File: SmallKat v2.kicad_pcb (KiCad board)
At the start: 4 copper layers, 104 x 56 mm, 272 parts, among them IC1 TPS562201DDCR, IC2 TPS40192DRCT, IC4 MAX34409ETE+, IC5 MAX34409ETE+, IC6 MAX34409ETE+, IC7 MAX34409ETE+, J1 Conn_01x03_Male, J10 Conn_01x03_Male, J11 Conn_01x03_Male, J12 Conn_01x03_Male, J13 Conn_01x03_Male, J14 Conn_01x03_Male, J15 Conn_01x03_Male, J16 Conn_01x03_Male, J17 Conn_01x03_Male, J19 USB_C_Receptacle, J2 Conn_01x03_Male, J21 Conn_01x05_Male, J3 Conn_01x03_Male, J4 Conn_01x03_Male, J5 Conn_01x03_Male, J6 Conn_01x03_Male, J7 Conn_01x03_Male, J8 Conn_01x03_Male, J9 Conn_01x02_Male, Q1 BUK9M120-100EX, Q10 CSD17307Q5A, Q11 CSD17307Q5A, Q12 Si7141DP, Q2 BUK9M120-100EX, Q3 MMBT3904, Q4 MMBT3904, Q7 2N3905, Q8 BUK9M120-100EX, Q9 BUK9M120-100EX, SW1 SW_SPST, SW2 SW_SPST, SW5 SW_SPST, U1 BNO055, U11 FUSB302BMPX, U12 BQ24770, U13 bq76925, U14 PCA9641, U2 LM2840Y, U3 ESP32-WROOM-32, U4 CP2102N-A01-GQFN24, U6 STM32L432KBUx, Y1 32.768kHz

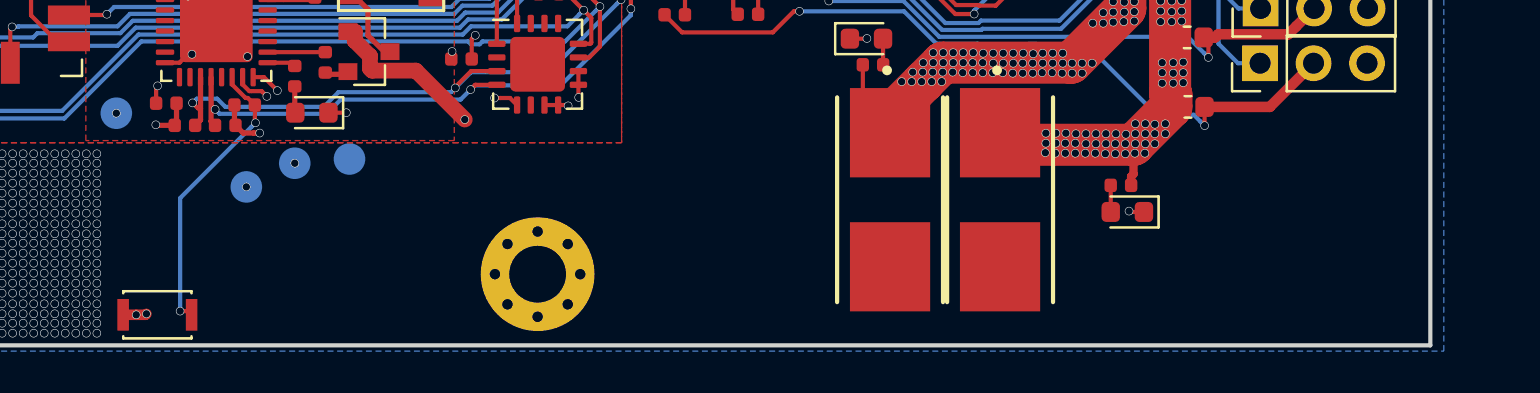
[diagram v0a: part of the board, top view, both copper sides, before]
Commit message: added version to silk
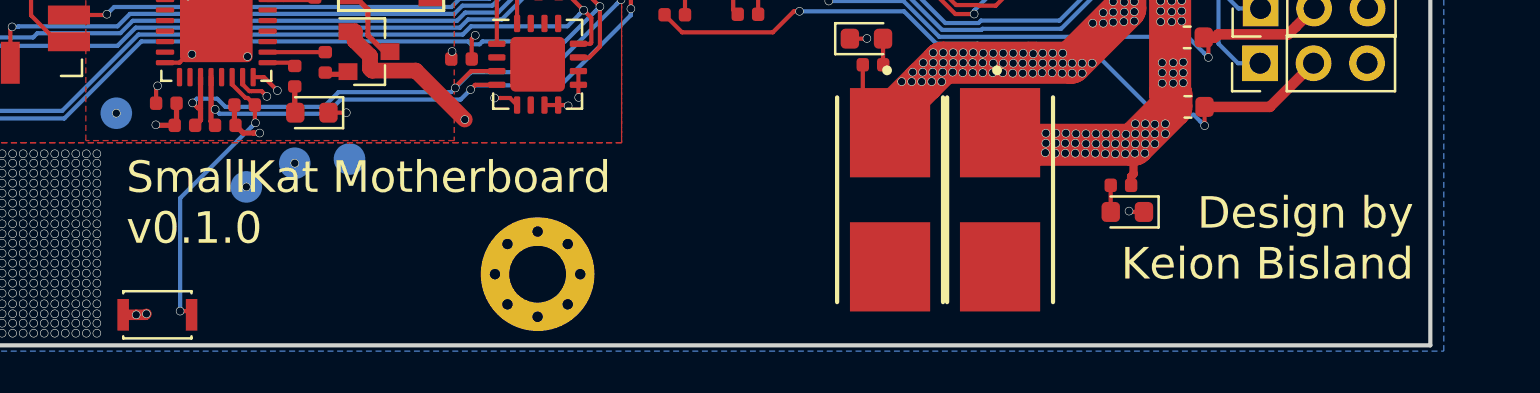
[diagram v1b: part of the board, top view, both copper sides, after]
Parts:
- L2: footprint Inductor_SMD:L_Bourns_SRP1245A -> L_Bourns_SRP1245A:L_Bourns_SRP1245A
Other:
- board text added: "Design by Keion Bisland"
- board text added: "SmallKat Motherboard v0.1.0"
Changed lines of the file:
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@@
   (general
     (thickness 1.6)
-    (drawings 23)
+    (drawings 25)
     (tracks 5690)
     (zones 0)
@@
       (drillshape 0)
       (scaleselection 1)
-      (outputdirectory "GERBER/"))
+      (outputdirectory "GERBER-t/"))
   )
   (net 0 "")
@@
     (add_net VBUS)
   )
+  (module L_Bourns_SRP1245A:L_Bourns_SRP1245A (layer F.Cu)
+    (at 135.8 94.3 180)
+    (descr "Bourns SRP1245A series SMD inductor http://www.bourns.com/docs/Product-Datasheets/SRP1245A.pdf")
+    (tags "Bourns SRP1245A SMD inductor")
+    (attr smd)
+    (fp_text reference L2 (at 0 -7.25 unlocked) (layer F.SilkS) hide
+      (effects (font (size 1 1) (thickness 0.15)))
+    )
+    (fp_text value 1uH (at 0 7.4 unlocked) (layer F.Fab) hide
+      (effects (font (size 1 1) (thickness 0.15)))
+    )
+    (fp_line (start -7.35 -2.75) (end -6.55 -2.75) (layer F.CrtYd) (width 0.05))
+    (fp_line (start -6.55 5.7) (end -6.55 2.75) (layer F.CrtYd) (width 0.05))
+    (fp_line (start -6.55 -2.75) (end -6.55 -5.7) (layer F.CrtYd) (width 0.05))
+    (fp_line (start -7.35 2.75) (end -6.55 2.75) (layer F.CrtYd) (width 0.05))
+    (fp_line (start -7.35 2.75) (end -7.35 -2.75) (layer F.CrtYd) (width 0.05))
+    (fp_line (start 6.55 2.75) (end 6.55 5.7) (layer F.CrtYd) (width 0.05))
+    (fp_line (start 6.55 -5.7) (end 6.55 -2.75) (layer F.CrtYd) (width 0.05))
+    (fp_line (start 7.35 -2.75) (end 7.35 2.75) (layer F.CrtYd) (width 0.05))
+    (fp_line (start 7.35 -2.75) (end 6.55 -2.75) (layer F.CrtYd) (width 0.05))
+    (fp_line (start 7.35 2.75) (end 6.55 2.75) (layer F.CrtYd) (width 0.05))
+    (fp_line (start -5.75 -6.25) (end 5.75 -6.25) (layer F.Fab) (width 0.1))
+    (fp_line (start -6.3 -5.75) (end -6.3 5.7) (layer F.Fab) (width 0.1))
+    (fp_line (start 5.75 6.25) (end -5.75 6.25) (layer F.Fab) (width 0.1))
+    (fp_line (start 6.3 -5.7) (end 6.3 5.7) (layer F.Fab) (width 0.1))
+    (fp_line (start -5.75 -6.4) (end 5.75 -6.4) (layer F.SilkS) (width 0.12))
+    (fp_line (start -6.45 -5.75) (end -6.45 -2.8) (layer F.SilkS) (width 0.12))
+    (fp_line (start 5.75 6.4) (end -5.75 6.4) (layer F.SilkS) (width 0.12))
+    (fp_line (start 6.45 -5.7) (end 6.45 -2.8) (layer F.SilkS) (width 0.12))
+    (fp_line (start -5.75 -6.5) (end 5.75 -6.5) (layer F.CrtYd) (width 0.05))
+    (fp_line (start 5.75 6.5) (end -5.75 6.5) (layer F.CrtYd) (width 0.05))
+    (fp_text user %R (at 0 0 unlocked) (layer F.Fab) hide
+      (effects (font (size 1 1) (thickness 0.15)))
+    )
+    (fp_arc (start -5.75 -5.7) (end -5.75 -6.25) (angle -90) (layer F.Fab) (width 0.1))
+    (fp_arc (start 5.75 -5.7) (end 6.3 -5.7) (angle -90) (layer F.Fab) (width 0.1))
+    (fp_arc (start 5.75 5.7) (end 5.75 6.25) (angle -90) (layer F.Fab) (width 0.1))
+    (fp_arc (start -5.75 5.7) (end -6.3 5.7) (angle -90) (layer F.Fab) (width 0.1))
+    (fp_line (start -6.45 2.8) (end -6.45 5.7) (layer F.SilkS) (width 0.12))
+    (fp_line (start 6.45 2.8) (end 6.45 5.7) (layer F.SilkS) (width 0.12))
+    (fp_arc (start -5.75 -5.7) (end -5.75 -6.4) (angle -90) (layer F.SilkS) (width 0.12))
+    (fp_arc (start -5.75 5.7) (end -6.45 5.7) (angle -90) (layer F.SilkS) (width 0.12))
+    (fp_arc (start 5.75 5.7) (end 5.75 6.4) (angle -90) (layer F.SilkS) (width 0.12))
+    (fp_arc (start 5.75 -5.7) (end 6.45 -5.7) (angle -90) (layer F.SilkS) (width 0.12))
+    (fp_arc (start -5.75 -5.7) (end -5.75 -6.5) (angle -90) (layer F.CrtYd) (width 0.05))
+    (fp_arc (start -5.75 5.7) (end -6.55 5.7) (angle -90) (layer F.CrtYd) (width 0.05))
+    (fp_arc (start 5.75 5.7) (end 5.75 6.5) (angle -90) (layer F.CrtYd) (width 0.05))
+    (fp_arc (start 5.75 -5.7) (end 6.55 -5.7) (angle -90) (layer F.CrtYd) (width 0.05))
+    (pad 2 smd rect (at 6.5 0 180) (size 3.1 5) (layers F.Cu F.Paste F.Mask)
+      (net 4 +6V))
+    (pad 1 smd rect (at -6.5 0 180) (size 3.1 5) (layers F.Cu F.Paste F.Mask)
+      (net 22 "Net-(C15-Pad1)"))
+    (model ${KISYS3DMOD}/Inductor_SMD.3dshapes/L_Bourns_SRP1245A.wrl
+      (at (xyz 0 0 0))
+      (scale (xyz 1 1 1))
+      (rotate (xyz 0 0 0))
+    )
+    (model "${KIPRJMOD}/L_Bourns_SRP1245A/SRP1245A series.stp"
+      (at (xyz 0 0 0))
+      (scale (xyz 1 1 1))
+      (rotate (xyz 0 0 0))
+    )
+  )
   (module USB_C_Receptacle_Amphenol_12401610E4-2A:USB_C_Receptacle_Amphenol_12401610E4-2A_CircularHoles (layer F.Cu)
     (at 171.18 92.09 180)
@@
       (rotate (xyz 0 0 0))
     )
+    (model ${KIPRJMOD}/USB_C_Receptacle_Amphenol_12401610E4-2A/12401610E4#2A--3DModel-STEP-56544.STEP
+      (offset (xyz 0 -5.25 1.5))
+      (scale (xyz 1 1 1))
+      (rotate (xyz -90 0 0))
+    )
   )
   (module 0154:0154.250DR (layer F.Cu)
@@
     (pad "" smd rect (at 1.95 -1.65) (size 1.2 0.7) (layers F.Cu F.Paste F.Mask))
   )
-  (module Inductor_SMD:L_Bourns_SRP1245A (layer F.Cu)
-    (at 135.8 94.3 180)
-    (descr "Bourns SRP1245A series SMD inductor http://www.bourns.com/docs/Product-Datasheets/SRP1245A.pdf")
-    (tags "Bourns SRP1245A SMD inductor")
-    (attr smd)
-    (fp_text reference L2 (at 0 -7.25 unlocked) (layer F.SilkS) hide
-      (effects (font (size 1 1) (thickness 0.15)))
-    )
-    (fp_text value 1uH (at 0 7.4 unlocked) (layer F.Fab) hide
-      (effects (font (size 1 1) (thickness 0.15)))
-    )
-    (fp_line (start -7.35 -2.75) (end -6.55 -2.75) (layer F.CrtYd) (width 0.05))
-    (fp_line (start -6.55 5.7) (end -6.55 2.75) (layer F.CrtYd) (width 0.05))
-    (fp_line (start -6.55 -2.75) (end -6.55 -5.7) (layer F.CrtYd) (width 0.05))
-    (fp_line (start -7.35 2.75) (end -6.55 2.75) (layer F.CrtYd) (width 0.05))
-    (fp_line (start -7.35 2.75) (end -7.35 -2.75) (layer F.CrtYd) (width 0.05))
-    (fp_line (start 6.55 2.75) (end 6.55 5.7) (layer F.CrtYd) (width 0.05))
-    (fp_line (start 6.55 -5.7) (end 6.55 -2.75) (layer F.CrtYd) (width 0.05))
-    (fp_line (start 7.35 -2.75) (end 7.35 2.75) (layer F.CrtYd) (width 0.05))
-    (fp_line (start 7.35 -2.75) (end 6.55 -2.75) (layer F.CrtYd) (width 0.05))
-    (fp_line (start 7.35 2.75) (end 6.55 2.75) (layer F.CrtYd) (width 0.05))
-    (fp_line (start -5.75 -6.25) (end 5.75 -6.25) (layer F.Fab) (width 0.1))
-    (fp_line (start -6.3 -5.75) (end -6.3 5.7) (layer F.Fab) (width 0.1))
-    (fp_line (start 5.75 6.25) (end -5.75 6.25) (layer F.Fab) (width 0.1))
-    (fp_line (start 6.3 -5.7) (end 6.3 5.7) (layer F.Fab) (width 0.1))
-    (fp_line (start -5.75 -6.4) (end 5.75 -6.4) (layer F.SilkS) (width 0.12))
-    (fp_line (start -6.45 -5.75) (end -6.45 -2.8) (layer F.SilkS) (width 0.12))
-    (fp_line (start 5.75 6.4) (end -5.75 6.4) (layer F.SilkS) (width 0.12))
-    (fp_line (start 6.45 -5.7) (end 6.45 -2.8) (layer F.SilkS) (width 0.12))
-    (fp_line (start -5.75 -6.5) (end 5.75 -6.5) (layer F.CrtYd) (width 0.05))
-    (fp_line (start 5.75 6.5) (end -5.75 6.5) (layer F.CrtYd) (width 0.05))
-    (fp_text user %R (at 0 0 unlocked) (layer F.Fab) hide
-      (effects (font (size 1 1) (thickness 0.15)))
-    )
-    (fp_arc (start -5.75 -5.7) (end -5.75 -6.25) (angle -90) (layer F.Fab) (width 0.1))
-    (fp_arc (start 5.75 -5.7) (end 6.3 -5.7) (angle -90) (layer F.Fab) (width 0.1))
-    (fp_arc (start 5.75 5.7) (end 5.75 6.25) (angle -90) (layer F.Fab) (width 0.1))
-    (fp_arc (start -5.75 5.7) (end -6.3 5.7) (angle -90) (layer F.Fab) (width 0.1))
-    (fp_line (start -6.45 2.8) (end -6.45 5.7) (layer F.SilkS) (width 0.12))
-    (fp_line (start 6.45 2.8) (end 6.45 5.7) (layer F.SilkS) (width 0.12))
-    (fp_arc (start -5.75 -5.7) (end -5.75 -6.4) (angle -90) (layer F.SilkS) (width 0.12))
-    (fp_arc (start -5.75 5.7) (end -6.45 5.7) (angle -90) (layer F.SilkS) (width 0.12))
-    (fp_arc (start 5.75 5.7) (end 5.75 6.4) (angle -90) (layer F.SilkS) (width 0.12))
-    (fp_arc (start 5.75 -5.7) (end 6.45 -5.7) (angle -90) (layer F.SilkS) (width 0.12))
-    (fp_arc (start -5.75 -5.7) (end -5.75 -6.5) (angle -90) (layer F.CrtYd) (width 0.05))
-    (fp_arc (start -5.75 5.7) (end -6.55 5.7) (angle -90) (layer F.CrtYd) (width 0.05))
-    (fp_arc (start 5.75 5.7) (end 5.75 6.5) (angle -90) (layer F.CrtYd) (width 0.05))
-    (fp_arc (start 5.75 -5.7) (end 6.55 -5.7) (angle -90) (layer F.CrtYd) (width 0.05))
-    (pad 2 smd rect (at 6.5 0 180) (size 3.1 5) (layers F.Cu F.Paste F.Mask)
-      (net 4 +6V))
-    (pad 1 smd rect (at -6.5 0 180) (size 3.1 5) (layers F.Cu F.Paste F.Mask)
-      (net 22 "Net-(C15-Pad1)"))
-    (model ${KISYS3DMOD}/Inductor_SMD.3dshapes/L_Bourns_SRP1245A.wrl
-      (at (xyz 0 0 0))
-      (scale (xyz 1 1 1))
-      (rotate (xyz 0 0 0))
-    )
-  )
   (module Resistor_SMD:R_0402_1005Metric (layer F.Cu)
     (at 140.39 107.775)
@@
     )
   )
+  (gr_text "Design by\nKeion Bisland" (at 202.17 137.8) (layer F.SilkS)
+    (effects (font (size 1.5 1.5) (thickness 0.3)) (justify right))
+  )
+  (gr_text "SmallKat Motherboard\nv0.1.0" (at 141.025 136.1) (layer F.SilkS)
+    (effects (font (size 1.5 1.5) (thickness 0.3)) (justify left))
+  )
   (gr_line (start 98.96 86.875) (end 202.96 86.875) (layer Edge.Cuts) (width 0.2))
